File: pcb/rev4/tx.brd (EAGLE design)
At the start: 28 x 36.5 mm, 55 parts, among them Q1 BSS84, U3 MCP73831T-2ACI/OT, Y1 CRYSTAL-26MHZSMD-3.2X2.5

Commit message: rev4 cleanup, new plate
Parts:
- moved R11 11.5 mm to (10.5, 1.65), turned to 270 degrees
- moved R10 11.5 mm to (8.84, 1.65), turned to 90 degrees
- moved R5 3.86 mm to (10.1, 4.85)
- moved R3 2.77 mm to (23.1, 6.43)
- moved R2 2.77 mm to (24.7, 6.43)
- moved U$4 2.44 mm to (13.5, 7.70)
- moved R9 0.99 mm to (24.2, 8.69), turned to 0 degrees
- moved LED1 0.74 mm to (8.61, 8.13)
- moved U3 0.36 mm to (7.06, 4.85)
- moved R4 0.31 mm to (5.46, 8.00)
- moved U$10 0.05 mm to (1.57, 21.6)
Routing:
- net N$35: track 8.75 -> 26.3 mm
- net GND: track 116.2 -> 101.3 mm
- net N$27: track 36.1 -> 22.1 mm
- net N$17: track 4.49 -> 1.74 mm
- net N$26: track 17.7 -> 20.0 mm
- net N$33: track 6.37 -> 8.66 mm
- net N$34: track 19.9 -> 18.9 mm
- net N$18: track 15.3 -> 14.7 mm
- net N$12: track 1.79 -> 2.42 mm
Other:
- board text added: "CH"
- board text added: "DFU"
- board text removed: "CAL"

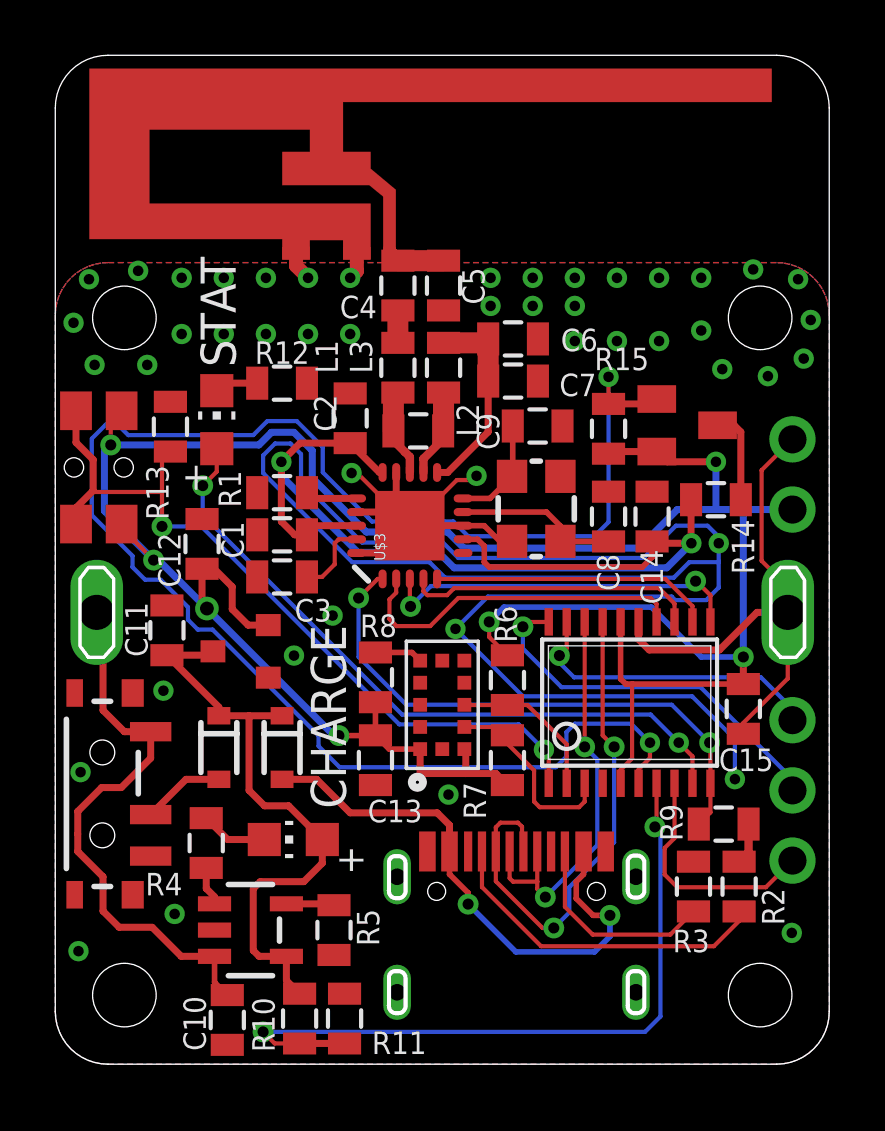
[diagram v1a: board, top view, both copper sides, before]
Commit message: added mounting hole plating
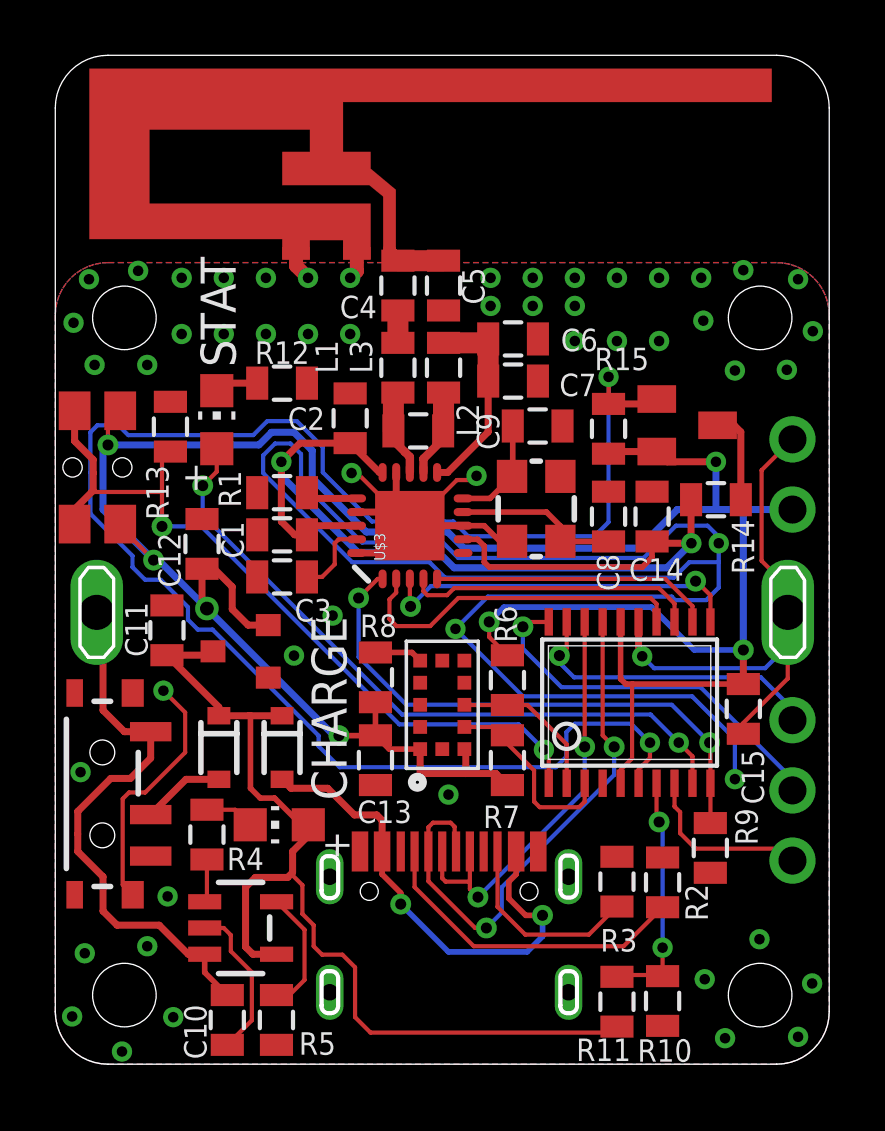
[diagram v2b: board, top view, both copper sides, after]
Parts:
- moved R11 11.5 mm to (22.0, 2.29), turned to 90 degrees
- moved R10 11.5 mm to (20.3, 2.26), turned to 270 degrees
- moved R5 3.86 mm to (8.00, 1.60)
- moved R3 2.77 mm to (20.3, 6.60)
- moved R2 2.77 mm to (22.0, 6.58)
- moved U$4 2.44 mm to (11.0, 7.70)
- moved R9 0.99 mm to (23.7, 7.82), turned to 270 degrees
- moved LED1 0.74 mm to (8.10, 8.66)
- moved U3 0.36 mm to (6.71, 4.93)
- moved R4 0.31 mm to (5.49, 8.31)
- moved U$10 0.05 mm to (1.52, 21.6)
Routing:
- net N$35: track 26.3 -> 8.75 mm
- net GND: track 101.3 -> 116.2 mm, vias 47 -> 55
- net N$27: track 22.1 -> 36.1 mm
- net N$17: track 1.74 -> 4.49 mm
- net N$26: track 20.0 -> 17.7 mm
- net N$33: track 8.66 -> 6.37 mm
- net N$34: track 18.9 -> 19.9 mm
- net N$18: track 14.7 -> 15.3 mm
- net N$12: track 2.42 -> 1.79 mm
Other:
- board text added: "CAL"
- board text added: "REV4 MAR2 19"
- board text removed: "CH"
- board text removed: "DFU"
- board text removed: "REV4 MAR19"
